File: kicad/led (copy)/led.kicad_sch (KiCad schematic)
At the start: 85 parts

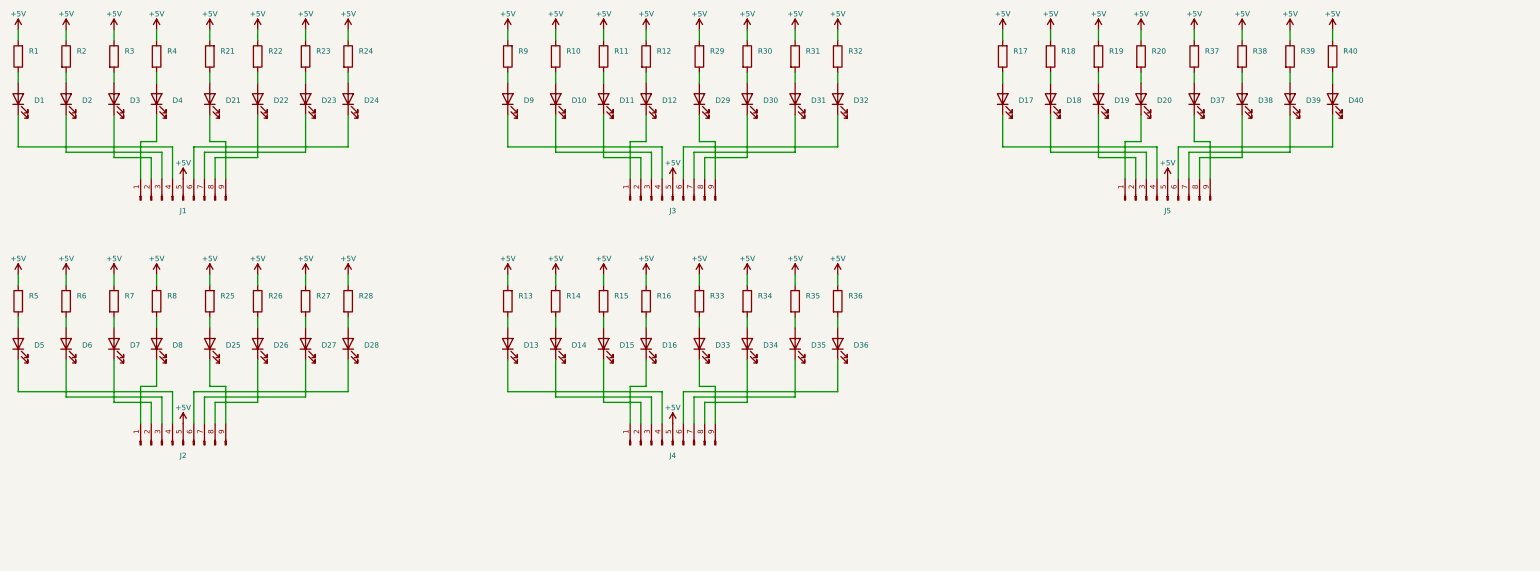
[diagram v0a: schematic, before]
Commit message: Copied LED board, and made new revision with full connectors, not split
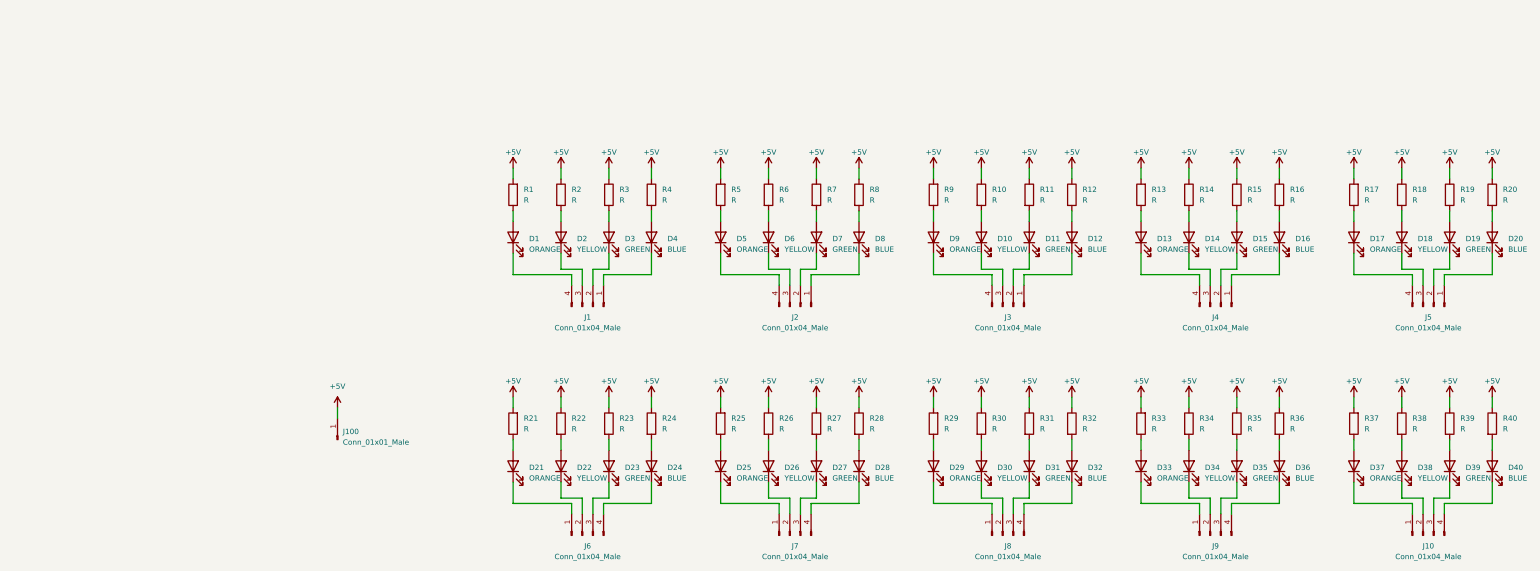
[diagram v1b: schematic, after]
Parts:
- removed J1, J2, J3, J4, J5: (no value), symbol Connector:Conn_01x09_Male
- added J1, J10, J2, J3, J4, J5, J6, J7, J8, J9: Conn_01x04_Male, Connector_PinHeader_2.54mm:PinHeader_1x04_P2.54mm_Horizontal, symbol Connector:Conn_01x04_Male
- added J100: Conn_01x01_Male, Connector_PinSocket_2.54mm:PinSocket_1x01_P2.54mm_Vertical, symbol Connector:Conn_01x01_Male
- D1, D13, D17, D21, D25, D29, D33, D37, D5, D9: value (none) -> ORANGE; footprint (none) -> LED_SMD:LED_1210_3225Metric
- D10, D14, D18, D2, D22, D26, D30, D34, D38, D6: value (none) -> YELLOW; footprint (none) -> LED_SMD:LED_1210_3225Metric
- D11, D15, D19, D23, D27, D3, D31, D35, D39, D7: value (none) -> GREEN; footprint (none) -> LED_SMD:LED_1210_3225Metric
- D12, D16, D20, D24, D28, D32, D36, D4, D40, D8: value (none) -> BLUE; footprint (none) -> LED_SMD:LED_1210_3225Metric
- R1, R10, R11, R12, R13, R14, R15, R16, R17, R18, R19, R2, R20, R21, R22, R23, R24, R25, R26, R27, R28, R29, R3, R30, R31, R32, R33, R34, R35, R36, R37, R38, R39, R4, R40, R5, R6, R7, R8, R9: value (none) -> R; footprint (none) -> Resistor_SMD:R_1206_3216Metric
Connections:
- net +5V: now also J100.1 (Pin_1)
- net at D14.1 (K): now also J4.3 (Pin_3)
- net at D18.1 (K): now also J5.3 (Pin_3)
- net at D4.1 (K): now also J1.1 (Pin_1)
- net at D11.1 (K): now also J3.2 (Pin_2)
- net at D8.1 (K): now also J2.1 (Pin_1)
- net at D15.1 (K): now also J4.2 (Pin_2)
- net at D22.1 (K): now also J6.2 (Pin_2)
- net at D12.1 (K): now also J3.1 (Pin_1)
- net at D10.1 (K): now also J3.3 (Pin_3)
- net at D9.1 (K): now also J3.4 (Pin_4)
- net at D32.1 (K): now also J8.4 (Pin_4)
- net at D31.1 (K): now also J8.3 (Pin_3)
- net at D30.1 (K): now also J8.2 (Pin_2)
- net at D29.1 (K): now also J8.1 (Pin_1)
- net at D26.1 (K): now also J7.2 (Pin_2)
- net at D2.1 (K): now also J1.3 (Pin_3)
- net at D36.1 (K): now also J9.4 (Pin_4)
- net at D39.1 (K): now also J10.3 (Pin_3)
- net at D19.1 (K): now also J5.2 (Pin_2)
- net at D16.1 (K): now also J4.1 (Pin_1)
- net at D20.1 (K): now also J5.1 (Pin_1)
- net at D5.1 (K): now also J2.4 (Pin_4)
- net at D34.1 (K): now also J9.2 (Pin_2)
- net at D40.1 (K): now also J10.4 (Pin_4)
- net at D6.1 (K): now also J2.3 (Pin_3)
- net at D3.1 (K): now also J1.2 (Pin_2)
- net at D7.1 (K): now also J2.2 (Pin_2)
- net at D28.1 (K): now also J7.4 (Pin_4)
- net at D27.1 (K): now also J7.3 (Pin_3)
- net at D25.1 (K): now also J7.1 (Pin_1)
- net at D17.1 (K): now also J5.4 (Pin_4)
- net at D38.1 (K): now also J10.2 (Pin_2)
- net at D37.1 (K): now also J10.1 (Pin_1)
- net at D23.1 (K): now also J6.3 (Pin_3)
- net at D1.1 (K): now also J1.4 (Pin_4)
- net at D24.1 (K): now also J6.4 (Pin_4)
- net at D21.1 (K): now also J6.1 (Pin_1)
- net at D35.1 (K): now also J9.3 (Pin_3)
- net at D13.1 (K): now also J4.4 (Pin_4)
- net at D33.1 (K): now also J9.1 (Pin_1)
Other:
- moved on the sheet: D1, D10, D11, D12, D13, D14, D15, D16, D17, D18, D19, D2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
